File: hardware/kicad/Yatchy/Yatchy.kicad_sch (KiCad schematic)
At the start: 92 parts, among them IC2 MCP23018-E_MJ, IC3 MCP73831T-2ATI_OT, J1 MOD_CONN, J10 MOD_CONN, J11 MOD_CONN, J12 MOD_CONN, J13 MOD_CONN, J14 MOD_CONN, J15 MOD_CONN, J16 MOD_CONN, J19 MOD_CONN, J2 MOD_CONN, J20 MOD_CONN, J21 MOD_CONN, J22 MOD_CONN, J23 MOD_CONN, J24 MOD_CONN, J25 MOD_CONN, J26 Conn_01x03_Pin, J27 MOD_CONN, J28 Conn_01x02_Pin, J3 MOD_CONN, J4 USB4730-GF-A-KIT, J5 SFV24R-4STBE1HLF, J6 MOD_CONN, J7 MOD_CONN, J8 MOD_CONN, J9 MOD_CONN, M1 Vibration_Motor, Q1 AO3400A, Q4 FDN304PZ, Q5 S8050, SW1 EVP-AKE31A, SW2 EVP-AKE31A, SW3 EVP-AKE31A, U1 USBLC6-2P6, U2 TLV75533PDBV, U3 ESP32-C6-MINI-1-N4, Y2 32.768KHz

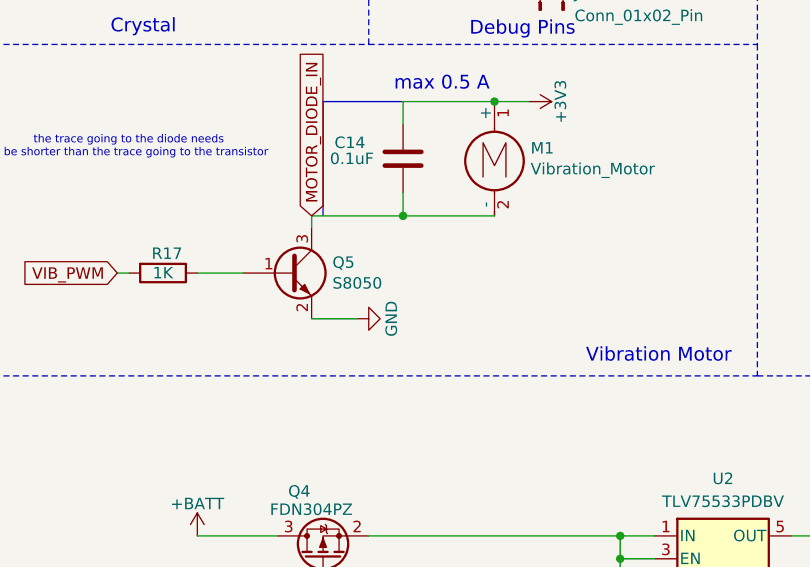
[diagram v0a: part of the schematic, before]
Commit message: change motor transistor name
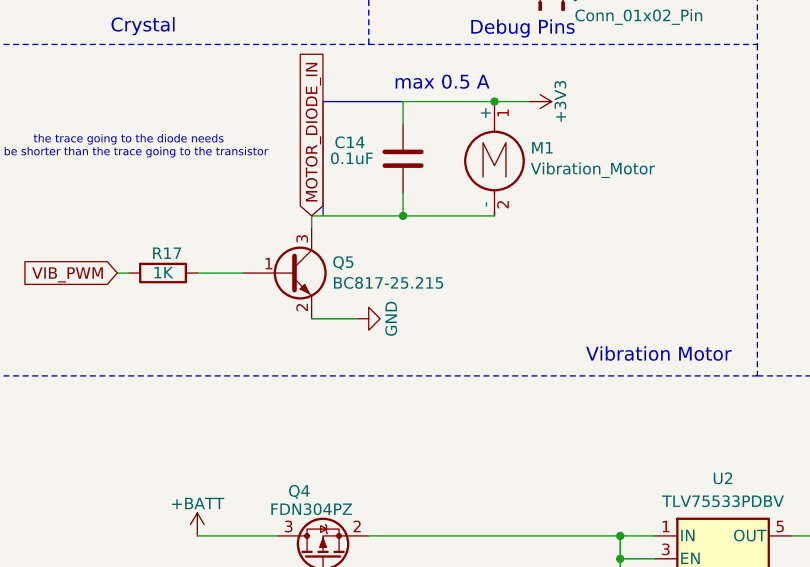
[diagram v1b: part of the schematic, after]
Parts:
- Q5: value S8050 -> BC817-25.215
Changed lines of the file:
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@@
 			)
 		)
-		(property "Value" "S8050"
+		(property "Value" "BC817-25.215"
 			(at 55.6514 218.313 0)
 			(effects

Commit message: change tvs diode fix module and calc
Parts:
- removed R12: 10K, Resistor_SMD:R_0402_1005Metric, symbol Watchy:R
- removed U1: USBLC6-2P6, Yatchy:SOT-666, symbol Watchy:USBLC6-2P6
- added D1, D3, D4: D_TVS, Diode_SMD:D_SOD-523, symbol Device:D_TVS
- R1, R2: value 5.1k -> 100k
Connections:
- net +3V3: now also IC2.12 (~{RESET})
- net DN: now also D3.1 (A1)
- net DP: now also D1.1 (A1)
- net GND: now also D1.2 (A2), D3.2 (A2), D4.2 (A2)
- net VBUS: now also D4.1 (A1)
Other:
- moved on the sheet: C21

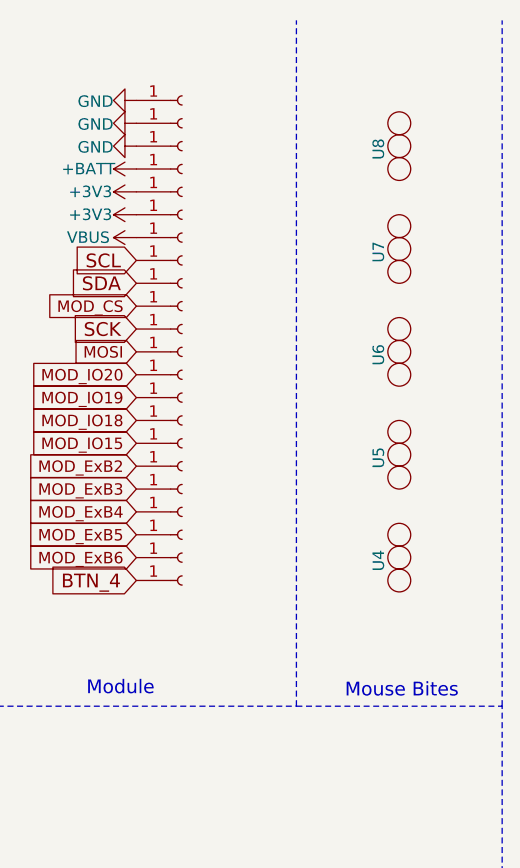
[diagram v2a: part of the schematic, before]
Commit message: remove mouse bites
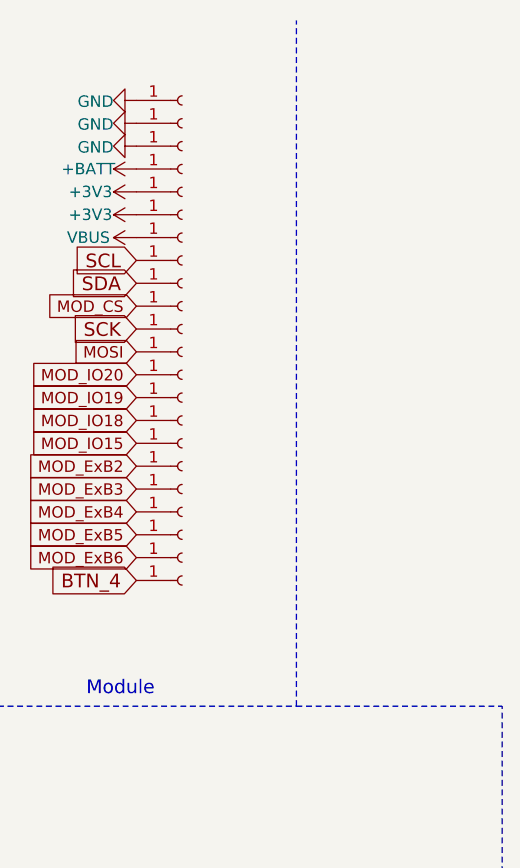
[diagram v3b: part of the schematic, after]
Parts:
- removed U4, U5, U6, U7, U8: ~, Yatchy:mouse-bite-3mm-slot, symbol Watchy:mouse_bite
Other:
- note removed: "Mouse Bites"

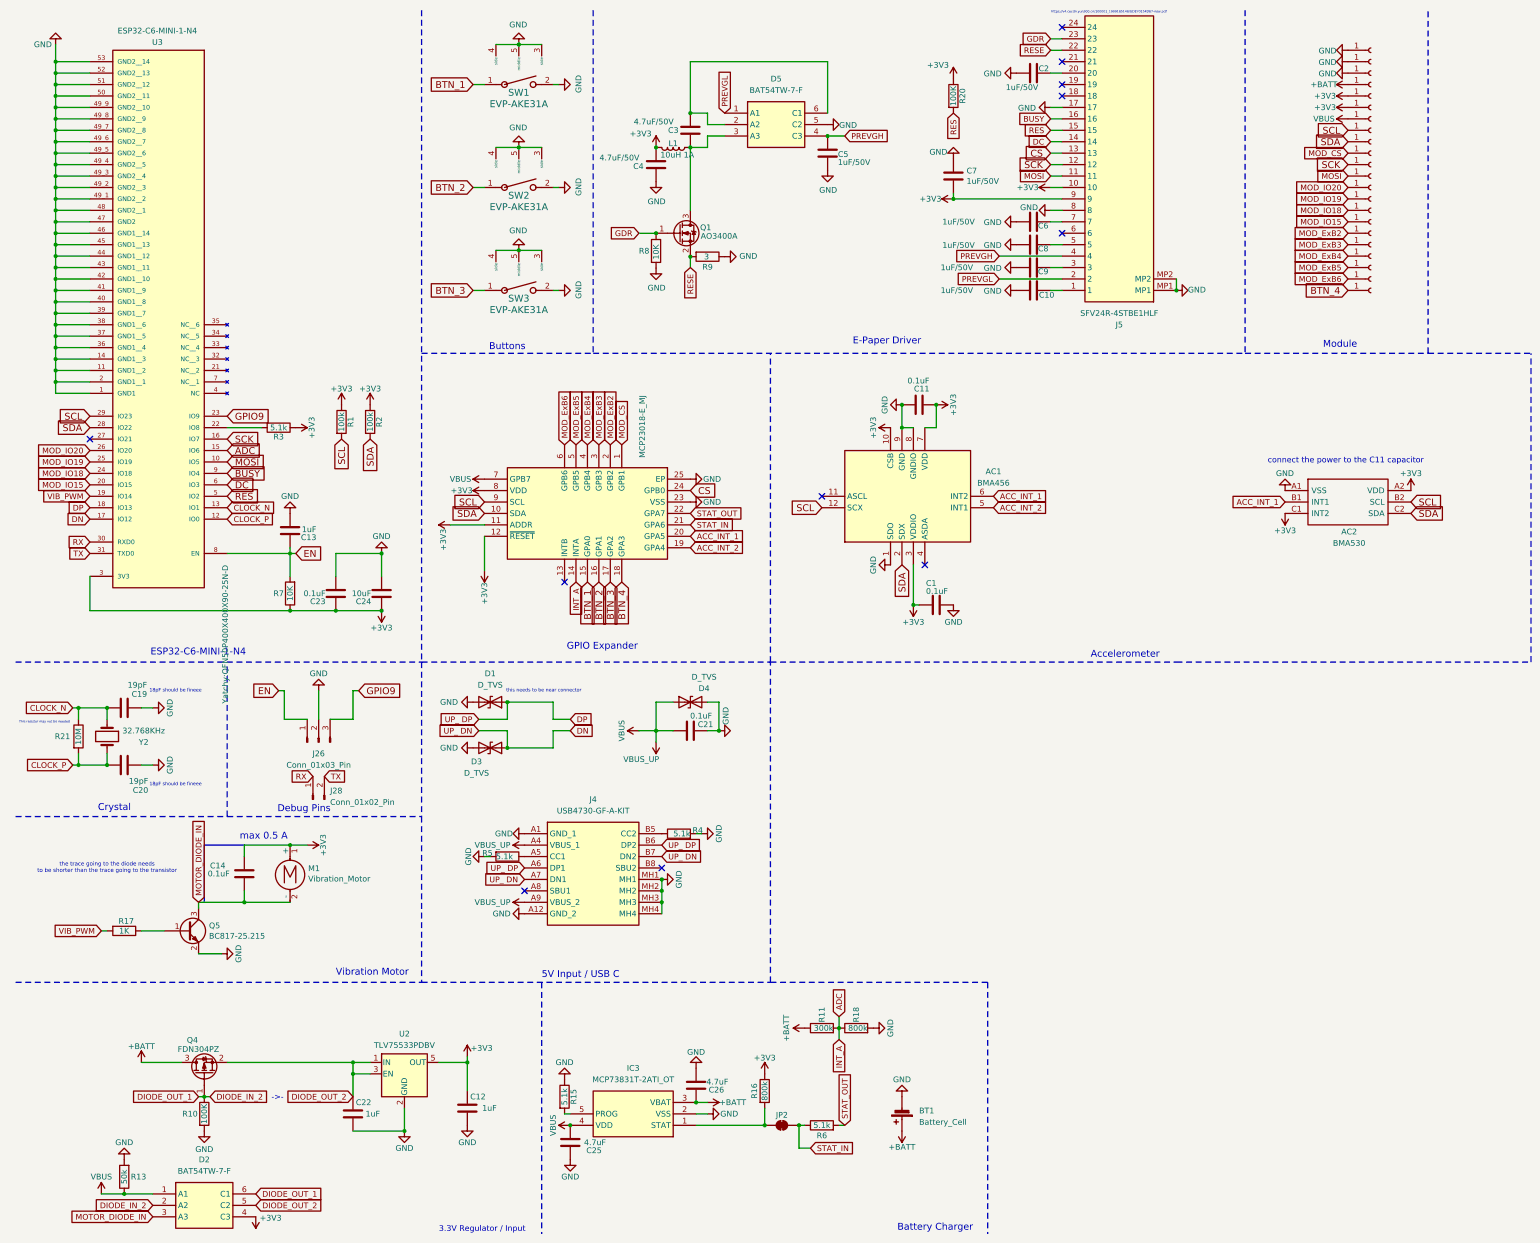
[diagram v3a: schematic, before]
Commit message: fix components-calc based on bom file, add 1K resistor to gpio expander 5V connection, change 50K resistor to 100K
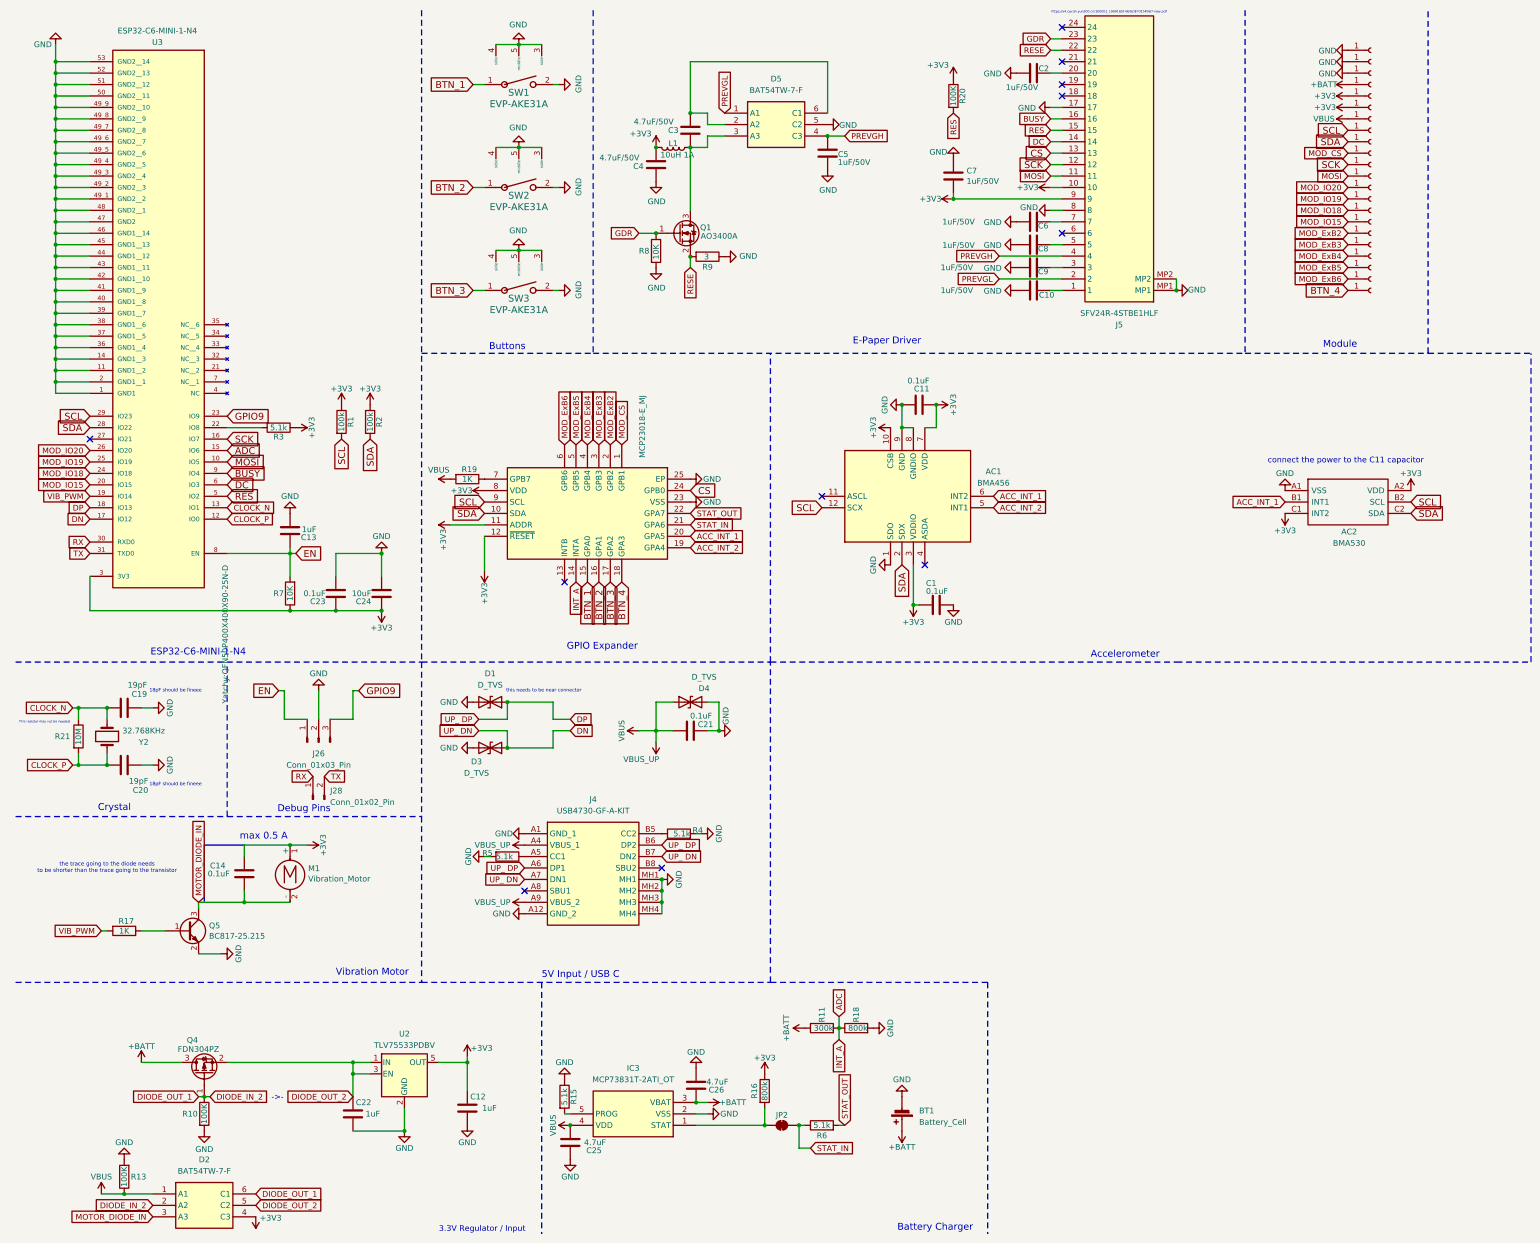
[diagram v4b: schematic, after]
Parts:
- added R19: 1K, Resistor_SMD:R_0402_1005Metric, symbol Watchy:R
- R13: value 50k -> 100K
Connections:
- net VBUS: now also R19.2; no longer IC2.7 (GPB7)
- new net: IC2.7 (GPB7), R19.1

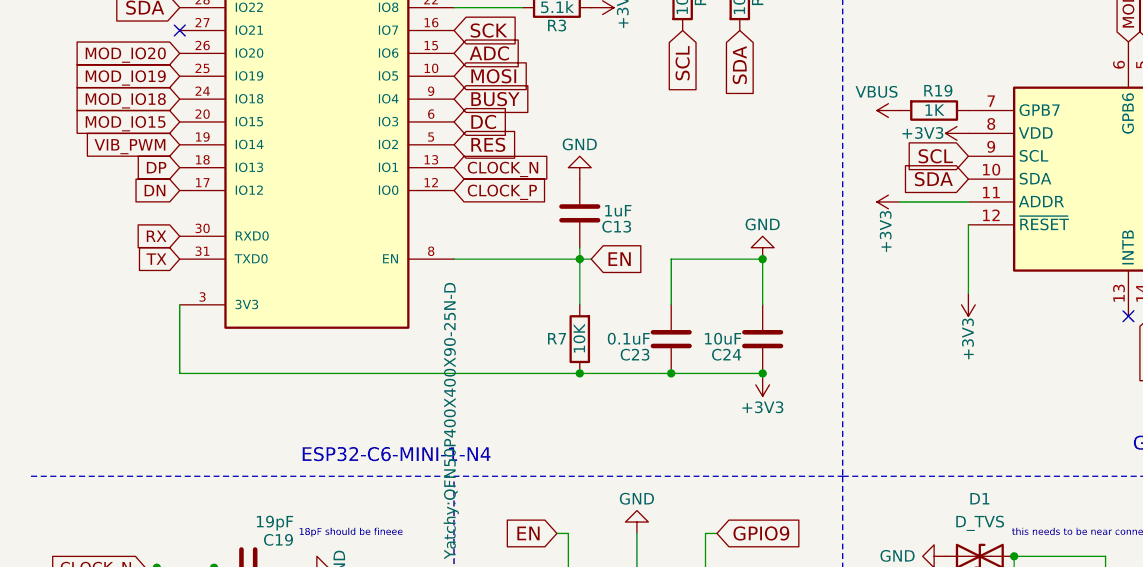
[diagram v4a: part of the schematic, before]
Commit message: connect mcp reset pin with esp32c6
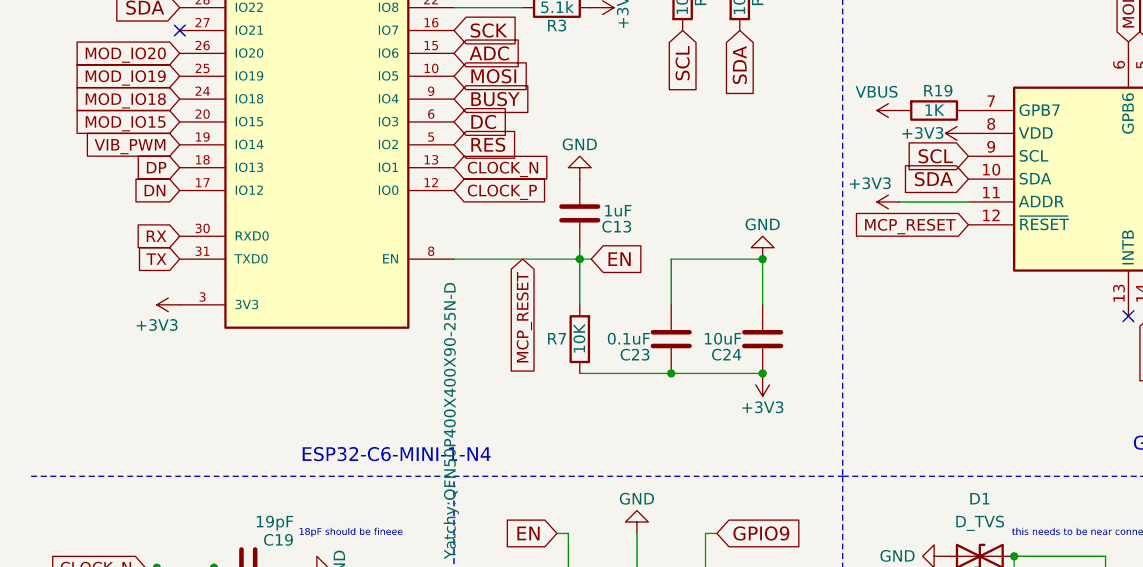
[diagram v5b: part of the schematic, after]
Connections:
- net +3V3: no longer IC2.12 (~{RESET})
- net EN: now also IC2.12 (~{RESET})
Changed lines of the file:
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@@
 	)
 	(junction
-		(at 73.66 146.05)
-		(diameter 0)
-		(color 0 0 0 0)
-	)
-	(junction
 		(at 121.92 176.53)
 		(diameter 0)
@@
 	(wire
 		(pts
-			(xy 29.21 138.43) (xy 29.21 146.05)
-		)
-		(stroke
-			(width 0)
-			(type default)
-		)
-	)
-	(wire
-		(pts
 			(xy 242.57 64.77) (xy 245.11 64.77)
 		)
@@
 	(wire
 		(pts
-			(xy 116.84 129.54) (xy 116.84 137.16)
-		)
-		(stroke
-			(width 0)
-			(type default)
-		)
-	)
-	(wire
-		(pts
 			(xy 133.35 52.07) (xy 132.08 52.07)
 		)
@@
 		)
 	)
-	(wire
-		(pts
-			(xy 29.21 146.05) (xy 73.66 146.05)
-		)
-		(stroke
-			(width 0)
-			(type default)
-		)
-	)
 	(global_label "MOD_ExB2"
 		(shape input)
@@
 		)
 	)
+	(global_label "MCP_RESET"
+		(shape input)
+		(at 116.84 129.54 180)
+		(fields_autoplaced yes)
+		(effects
+			(font
+				(size 1.27 1.27)
+			)
+			(justify right)
+		)
+		(property "Intersheetrefs" "${INTERSHEET_REFS}"
+			(at 103.8049 129.54 0)
+			(effects
+				(font
+					(size 1.27 1.27)
+				)
+				(justify right)
+				(hide yes)
+			)
+		)
+	)
 	(global_label "TX"
 		(shape input)
@@
 		)
 	)
+	(global_label "MCP_RESET"
+		(shape input)
+		(at 67.31 133.35 270)
+		(fields_autoplaced yes)
+		(effects
+			(font
+				(size 1.27 1.27)
+			)
+			(justify right)
+		)
+		(property "Intersheetrefs" "${INTERSHEET_REFS}"
+			(at 67.31 146.3851 90)
+			(effects
+				(font
+					(size 1.27 1.27)
+				)
+				(justify right)
+				(hide yes)
+			)
+		)
+	)
 	(global_label "DIODE_IN_2"
 		(shape input)
@@
 	(symbol
 		(lib_id "Watchy:+3V3-power")
-		(at 116.84 137.16 180)
-		(unit 1)
-		(exclude_from_sim no)
-		(in_bom yes)
-		(on_board yes)
-		(dnp no)
-		(property "Reference" "#PWR08"
-			(at 116.84 133.35 0)
-			(effects
-				(font
-					(size 1.27 1.27)
-				)
-				(hide yes)
-			)
-		)
-		(property "Value" "+3V3"
-			(at 116.84 142.24 90)
-			(effects
-				(font
-					(size 1.27 1.27)
-				)
-			)
-		)
-		(property "Footprint" ""
-			(at 116.84 137.16 0)
-			(effects
-				(font
-					(size 1.27 1.27)
-				)
-				(hide yes)
-			)
-		)
-		(property "Datasheet" ""
-			(at 116.84 137.16 0)
-			(effects
-				(font
-					(size 1.27 1.27)
-				)
-				(hide yes)
-			)
-		)
-		(property "Description" ""
-			(at 116.84 137.16 0)
-			(effects
-				(font
-					(size 1.27 1.27)
-				)
-				(hide yes)
-			)
-		)
-		(pin "1"
-		)
-		(instances
-			(project "Watchy"
-				(path "/f041cf41-3a16-4080-b1fe-997266120697"
-					(reference "#PWR08")
-					(unit 1)
-				)
-			)
-		)
-	)
-	(symbol
-		(lib_id "Watchy:+3V3-power")
 		(at 212.09 144.78 180)
 		(unit 1)
@@
 	)
 	(symbol
+		(lib_id "Watchy:+3V3-power")
+		(at 29.21 138.43 90)
+		(unit 1)
+		(exclude_from_sim no)
+		(in_bom yes)
+		(on_board yes)
+		(dnp no)
+		(property "Reference" "#PWR08"
+			(at 33.02 138.43 0)
+			(effects
+				(font
+					(size 1.27 1.27)
+				)
+				(hide yes)
+			)
+		)
+		(property "Value" "+3V3"
+			(at 26.67 140.716 90)
+			(effects
+				(font
+					(size 1.27 1.27)
+				)
+			)
+		)
+		(property "Footprint" ""
+			(at 29.21 138.43 0)
+			(effects
+				(font
+					(size 1.27 1.27)
+				)
+				(hide yes)
+			)
+		)
+		(property "Datasheet" ""
+			(at 29.21 138.43 0)
+			(effects
+				(font
+					(size 1.27 1.27)
+				)
+				(hide yes)
+			)
+		)
+		(property "Description" ""
+			(at 29.21 138.43 0)
+			(effects
+				(font
+					(size 1.27 1.27)
+				)
+				(hide yes)
+			)
+		)
+		(pin "1"
+		)
+		(instances
+			(project "Yatchy"
+				(path "/f041cf41-3a16-4080-b1fe-997266120697"
+					(reference "#PWR08")
+					(unit 1)
+				)
+			)
+		)
+	)
+	(symbol
 		(lib_id "BMA530:BMA530")
 		(at 294.64 119.38 0)
@@
 		)
 		(property "Value" "+3V3"
-			(at 107.696 130.302 0)
+			(at 105.918 124.968 90)
 			(effects
 				(font

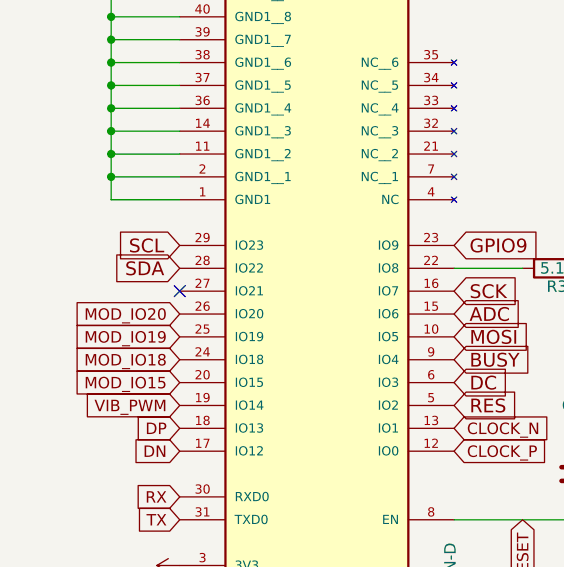
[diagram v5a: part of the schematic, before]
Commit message: Add screen, expose test point
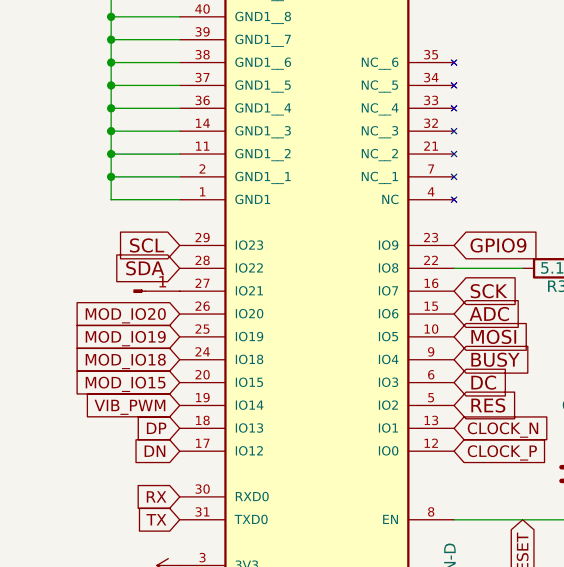
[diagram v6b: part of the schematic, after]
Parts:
- added J17: Conn_01x01_Pin, Yatchy:testpoint, symbol Connector:Conn_01x01_Pin
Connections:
- net at U3.27 (IO21): now also J17.1 (Pin_1)
- no-connect marks 11 -> 10
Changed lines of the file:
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@@
 	)
 	(no_connect
-		(at 29.21 107.95)
-	)
-	(no_connect
 		(at 125.73 208.28)
 	)
@@
 					(unit 1)
 				)
+			)
+		)
+	)
+	(symbol
+		(lib_id "Connector:Conn_01x01_Pin")
+		(at 24.13 107.95 0)
+		(unit 1)
+		(exclude_from_sim no)
+		(in_bom yes)
+		(on_board yes)
+		(dnp no)
+		(fields_autoplaced yes)
+		(property "Reference" "J17"
+			(at 24.765 102.87 0)
+			(effects
+				(font
+					(size 1.27 1.27)
+				)
+				(hide yes)
+			)
+		)
+		(property "Value" "Conn_01x01_Pin"
+			(at 24.765 105.41 0)
+			(effects
+				(font
+					(size 1.27 1.27)
+				)
+				(hide yes)
+			)
+		)
+		(property "Footprint" "Yatchy:testpoint"
+			(at 24.13 107.95 0)
+			(effects
+				(font
+					(size 1.27 1.27)
+				)
+				(hide yes)
+			)
+		)
+		(property "Datasheet" "~"
+			(at 24.13 107.95 0)
+			(effects
+				(font
+					(size 1.27 1.27)
+				)
+				(hide yes)
+			)
+		)
+		(property "Description" "Generic connector, single row, 01x01, script generated"
+			(at 24.13 107.95 0)
+			(effects
+				(font
+					(size 1.27 1.27)
+				)
+				(hide yes)
+			)
+		)
+		(pin "1"
+		)
+		(instances
+			(project ""
+				(path "/f041cf41-3a16-4080-b1fe-997266120697"
+					(reference "J17")
+					(unit 1)
+				)

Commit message: add new module
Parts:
- U2: footprint Package_TO_SOT_SMD:SOT-23-5 -> Yatchy:TLV75733PDYDR
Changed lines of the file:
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@@
 			)
 		)
-		(property "Footprint" "Package_TO_SOT_SMD:SOT-23-5"
+		(property "Footprint" "Yatchy:TLV75733PDYDR"
 			(at 99.06 240.665 0)
 			(effects
